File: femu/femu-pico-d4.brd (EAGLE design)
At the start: 24.1 x 15.8 mm, 54 parts, among them IC1 ESP32-QFN_5X5, IC3 FT230XQ

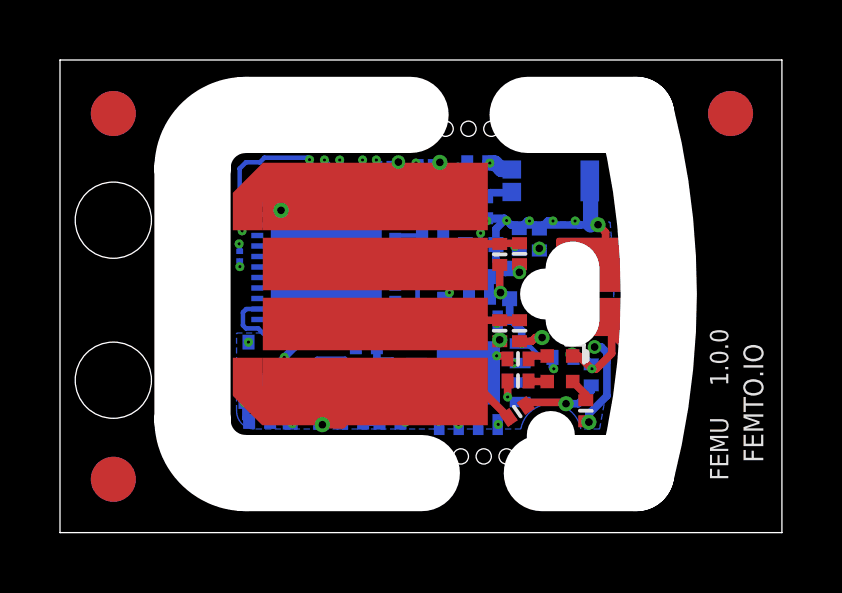
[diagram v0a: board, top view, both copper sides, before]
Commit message: Updating BoM to use the FT231XQ
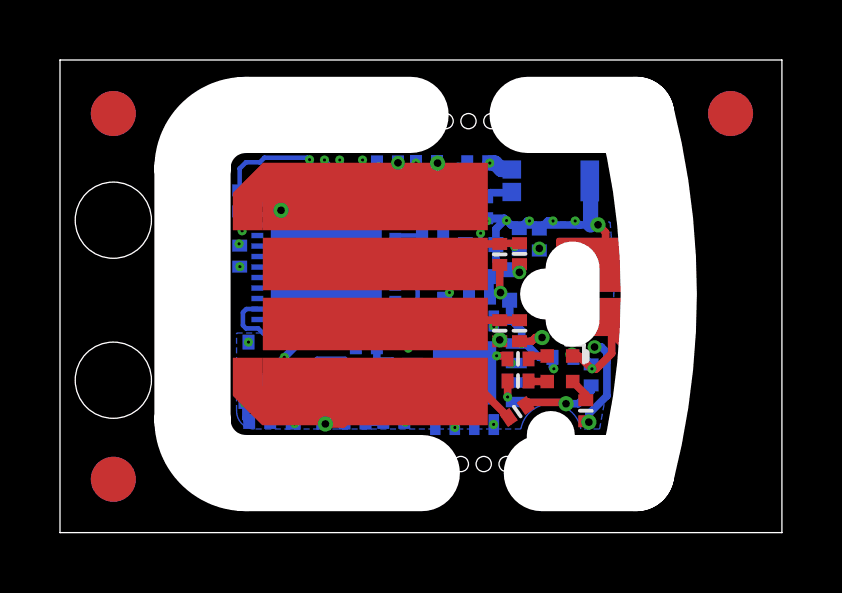
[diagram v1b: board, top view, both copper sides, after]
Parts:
- C13, C17, C20, R1: device parts_01005:01005 -> parts_0201:PART
- C4, C5: value 10pF -> 8pF
- moved C27 0.13 mm to (11.1, 3.71)
- moved IC3 0.13 mm to (13.5, 5.33)
- moved C20 0.11 mm to (10.9, 12.3)
- moved FB1 0.10 mm to (8.28, 3.68)
- moved C23 0.08 mm to (9.83, 3.68)
- moved C10 0.05 mm to (15.0, 8.26)
- renumbered ANT1 to U$11, LDO1 to U$33
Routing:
- net GND: track 73.4 -> 71.7 mm
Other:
- board text removed: "1.0.0"
- board text removed: "FEMTO.IO"
- board text removed: "FEMU"
